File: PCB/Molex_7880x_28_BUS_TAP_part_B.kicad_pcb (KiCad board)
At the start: 2 copper layers, 40.6 x 41.9 mm, 3 parts, among them J1 F52R-1A7H1-11028, J2 Molex_78805, J3 2x14_2.54mm_male_pins_horizon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

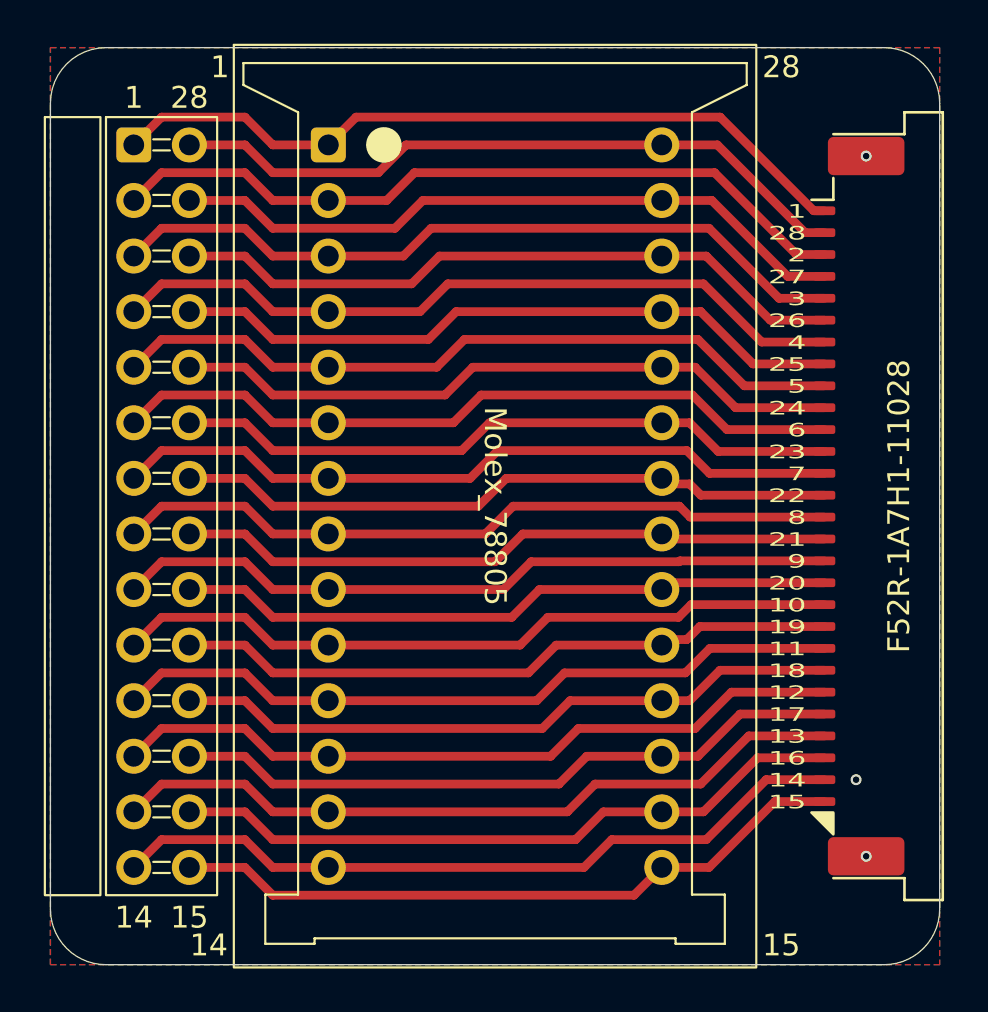
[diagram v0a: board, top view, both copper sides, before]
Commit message: add housing, add extra gnd pin
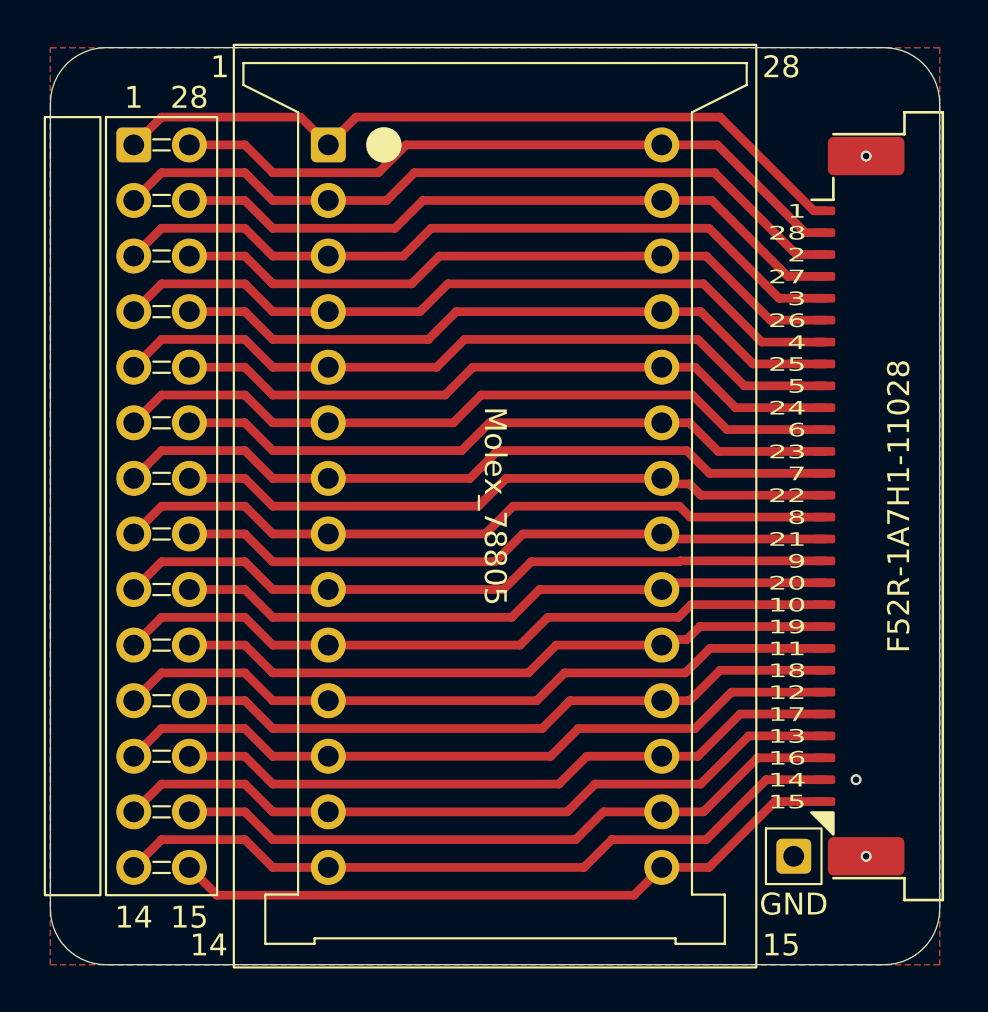
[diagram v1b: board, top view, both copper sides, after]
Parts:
- added J4: Conn_01x01_Pin, 000_LOCAL:PinHeader_1x1_P2.54mm, F.Cu at (156.0, 111.6)
- added N1: Housing, 000_LOCAL:Molex_7880x_bus_tap_cover, F.Cu at (142.4, 95.6)
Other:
- board text added: "GND"
